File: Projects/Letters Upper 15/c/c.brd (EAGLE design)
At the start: 16.5 x 21.6 mm, 37 parts

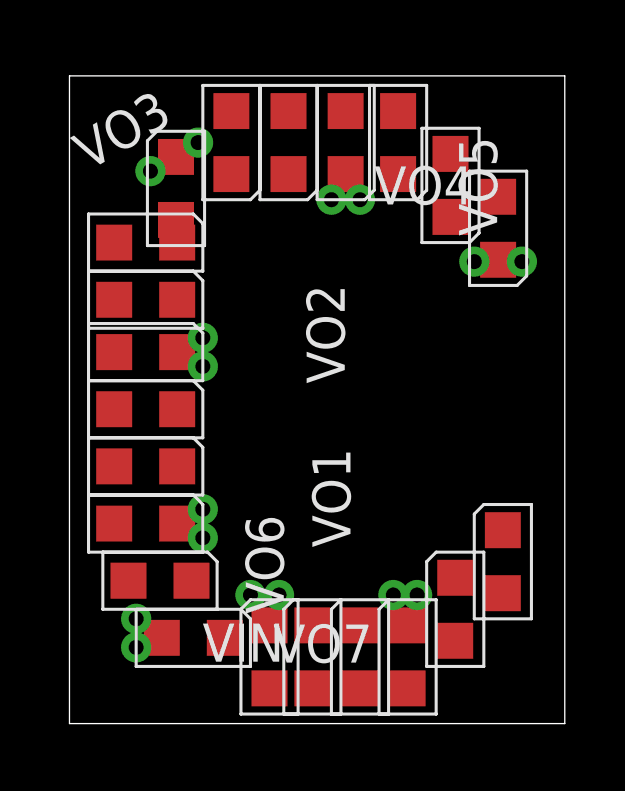
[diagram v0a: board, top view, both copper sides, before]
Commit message: 
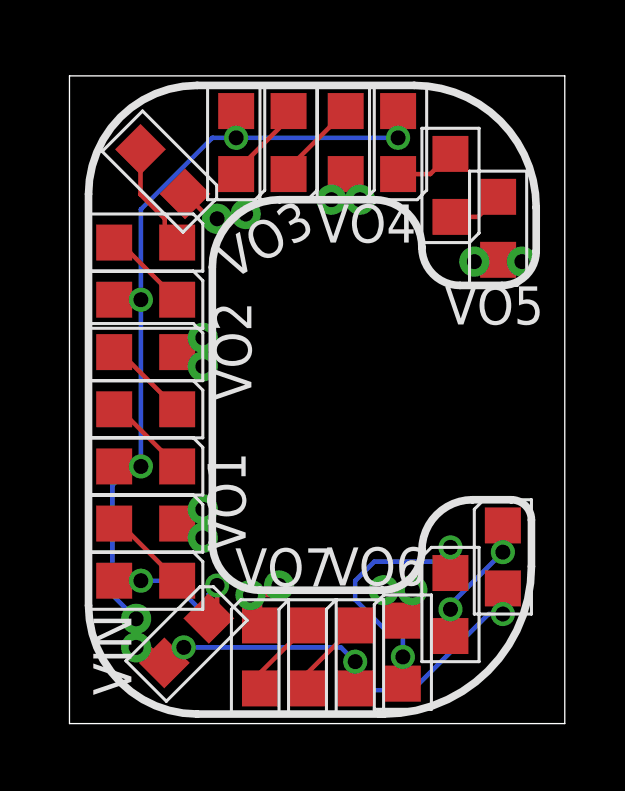
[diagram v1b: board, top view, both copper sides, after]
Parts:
- moved VO3 3.48 mm to (5.87, 17.0)
- moved VO10 2.62 mm to (4.92, 16.8)
- moved VO13 1.12 mm to (10.5, 4.45)
- moved LED9 0.71 mm to (3.11, 18.4), turned to 225 degrees
- moved VO6 0.65 mm to (11.4, 4.45)
- moved LED2 0.48 mm to (2.54, 4.76)
- moved LED21 0.32 mm to (6.35, 2.22)
- moved VO7 0.32 mm to (6.99, 4.60)
- moved LED1 0.24 mm to (3.90, 2.76), turned to 315 degrees
- moved LED17 0.22 mm to (12.7, 3.97)
- moved LED18 0.22 mm to (11.1, 2.38)
- moved LED19 0.17 mm to (9.52, 2.22)
- moved LED10 0.16 mm to (5.56, 19.4)
- moved LED16 0.16 mm to (14.4, 5.56)
- moved LED20 0.16 mm to (7.94, 2.22)
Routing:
- net VIN: track 0.00 -> 45.2 mm, vias 0 -> 7
- net N$23: track 0.00 -> 8.86 mm, vias 0 -> 2
- net N$4: track 0.00 -> 6.10 mm, vias 0 -> 2
- net N$24: track 0.00 -> 4.41 mm, vias 0 -> 2
- net N$11: track 0.00 -> 3.61 mm
- net N$16: track 0.00 -> 2.97 mm
- net N$7: track 0.00 -> 2.89 mm
- net N$15: track 0.00 -> 2.89 mm
- net N$12: track 0.00 -> 2.89 mm
- net N$3: track 0.00 -> 2.89 mm
- net N$8: track 0.00 -> 2.89 mm
- net N$27: track 0.00 -> 2.76 mm
- net N$28: track 0.00 -> 2.75 mm
- net VOUT3: track 0.00 -> 2.43 mm
- net VOUT6: track 0.00 -> 2.42 mm
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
